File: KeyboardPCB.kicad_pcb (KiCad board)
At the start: 2 copper layers, 400.1 x 116.7 mm, 236 parts

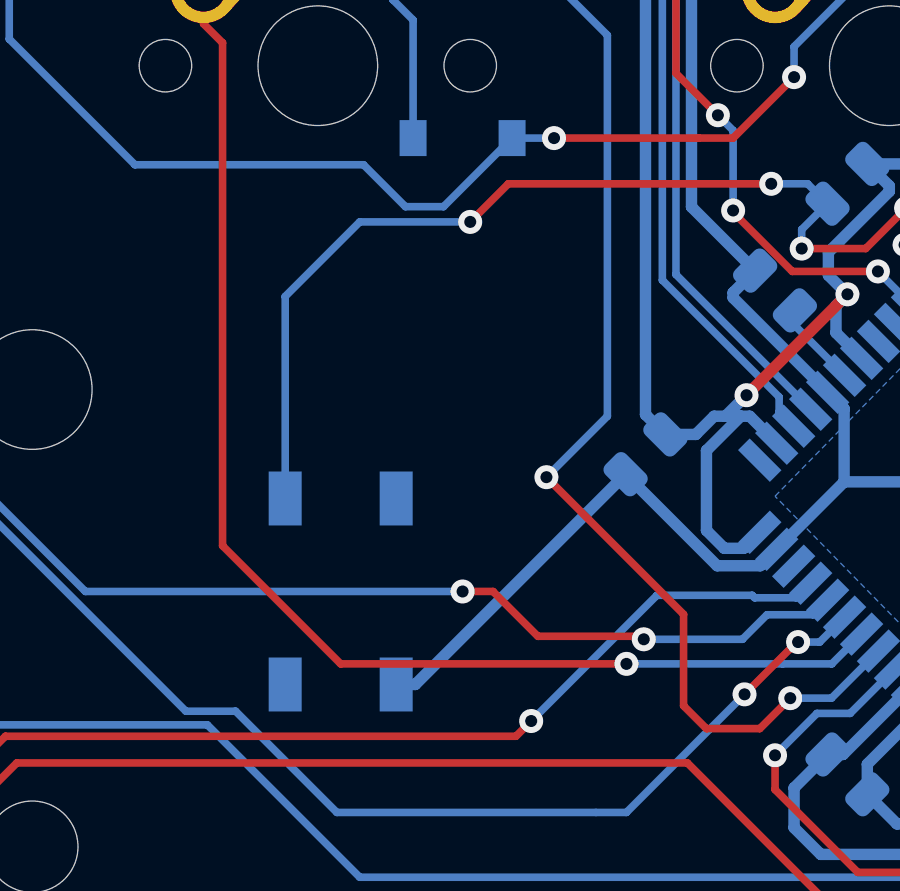
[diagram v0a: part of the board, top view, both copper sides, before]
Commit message: created custom library, added reset footprint to there
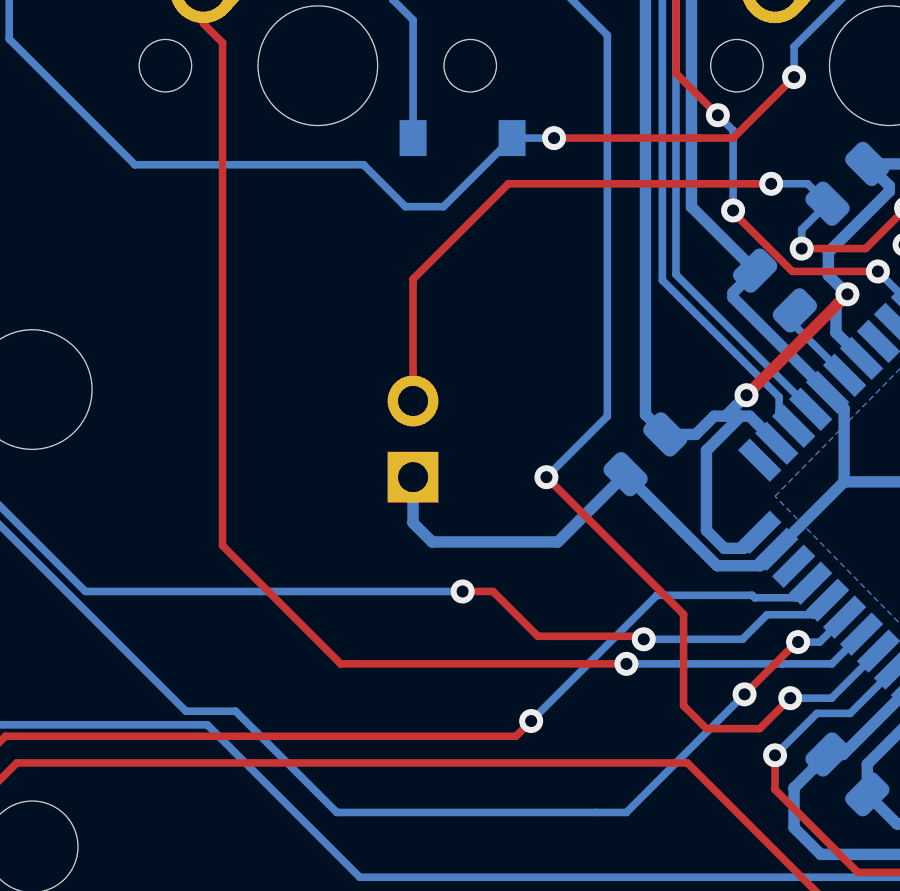
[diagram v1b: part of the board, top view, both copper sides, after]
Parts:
- SW_RESET1: footprint random-keyboard-parts:SKQG-1155865 -> random-keyboard-parts:Reset_Pretty_2pin
- moved SW_RESET1 5.08 mm to (127.6, 79.1)
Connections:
- SW_RESET1 pad 1: GND -> Net-(CONT1-Pad13)
- SW_RESET1 pad 2: Net-(CONT1-Pad13) -> GND
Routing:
- net Net-(CONT1-Pad13): track 40.5 -> 33.4 mm, vias 4 -> 3
- net GND: track 212.8 -> 212.0 mm

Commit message: fixes
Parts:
- SW_RESET1: footprint random-keyboard-parts:Reset_Pretty_2pin -> ErlMod:Reset_Pretty_2pin
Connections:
- SW_RESET1 pad 1: Net-(CONT1-Pad13) -> GND
- SW_RESET1 pad 2: GND -> Net-(CONT1-Pad13)
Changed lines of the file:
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@@
     (add_net VCC)
   )
-  (module random-keyboard-parts:Reset_Pretty_2pin (layer B.Cu)
+  (module ErlMod:Reset_Pretty_2pin (layer B.Cu)
     (at 127.635 79.121 270)
     (attr virtual)
@@
     (fp_line (start 2.5 -3.75) (end -2.5 -3.75) (layer B.SilkS) (width 0.25))
     (fp_line (start -2.5 -3.75) (end -2.5 -1.25) (layer B.SilkS) (width 0.25))
-    (pad 2 thru_hole rect (at 1.27 -2.54 270) (size 1.7 1.7) (drill 1) (layers *.Cu *.Mask)
+    (pad 1 thru_hole rect (at 1.27 -2.54 270) (size 1.7 1.7) (drill 1) (layers *.Cu *.Mask)
       (net 1 GND))
-    (pad 1 thru_hole circle (at -1.27 -2.54 270) (size 1.7 1.7) (drill 1) (layers *.Cu *.Mask)
+    (pad 2 thru_hole circle (at -1.27 -2.54 270) (size 1.7 1.7) (drill 1) (layers *.Cu *.Mask)
       (net 8 "Net-(CONT1-Pad13)"))
   )

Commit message: minor changes, added bom files
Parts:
- MX0:0_AFT1: value MX-NoLED -> MEDIA_AFT
- MX0:1_PLAY1: value MX-NoLED -> MEDIA_PLAY
- MX0:2_FWD1: value MX-NoLED -> MEDIA_FWD
- MX0:3_MUT1: value MX-NoLED -> MEDIA_MUTE
- MX0:4_VOL-1: value MX-NoLED -> MEDIA_VOLDN
- MX0:5_VOL+1: value MX-NoLED -> MEDIA_VOLUP
- MX0:6_ESC1: value MX-NoLED -> ESC
- MX0:7_F1: value MX-NoLED -> F1
- MX0:8_F2: value MX-NoLED -> F2
- MX0:9_F3: value MX-NoLED -> F3
- MX10:0_PGU1: value MX-NoLED -> PAGE_DOWN
- MX10:1_UP1: value MX-NoLED -> ARROW_UP
- MX10:4_RSH1: value MX-NoLED -> RIGHT_SHIFT
- MX10:5_/1: value MX-NoLED -> /
- MX10:6_.1: value MX-NoLED -> >
- MX10:7_,1: value MX-NoLED -> <
- MX10:8_M1: value MX-NoLED -> M
- MX10:9_N1: value MX-NoLED -> N
- MX11:0_RGT1: value MX-NoLED -> ARROW_RIGHT
- MX11:1_DWN1: value MX-NoLED -> ARROW_DOWN
- MX11:2_LFT1: value MX-NoLED -> ARROW_LEFT
- MX11:3_RCT1: value MX-NoLED -> RIGHT_CTRL
- MX11:4_MEN1: value MX-NoLED -> MENU
- MX11:5_OS1: value MX-NoLED -> RIGHT_OS
- MX11:6_AGR1: value MX-NoLED -> ALT_GR
- MX1:0_NUM1: value MX-NoLED -> NUM_LOCK
- MX1:1_NU/1: value MX-NoLED -> NUM_/
- MX1:2_NU*1: value MX-NoLED -> NUM_*
- MX1:3_NU-1: value MX-NoLED -> NUM_-
- MX1:4_TIL1: value MX-NoLED -> `
- MX1:5_1: value MX-NoLED -> 1
- MX1:6_2: value MX-NoLED -> 2
- MX1:7_3: value MX-NoLED -> 3
- MX1:8_4: value MX-NoLED -> 4
- MX1:9_5: value MX-NoLED -> 5
- MX2:0_NU7: value MX-NoLED -> NUM_7
- MX2:1_NU8: value MX-NoLED -> NUM_8
- MX2:2_NU9: value MX-NoLED -> NUM_9
- MX2:3_NU+1: value MX-NoLED -> NUM_+
- MX2:4_TAB1: value MX-NoLED -> TAB
- MX2:5_Q1: value MX-NoLED -> Q
- MX2:6_W1: value MX-NoLED -> W
- MX2:7_E1: value MX-NoLED -> E
- MX2:8_R1: value MX-NoLED -> R
- MX2:9_T1: value MX-NoLED -> T
- MX3:0_NU4: value MX-NoLED -> NUM_4
- MX3:1_NU5: value MX-NoLED -> NUM_5
- MX3:2_NU6: value MX-NoLED -> NUM_6
- MX3:4_CAP1: value MX-NoLED -> CAPS
- MX3:5_A1: value MX-NoLED -> A
- MX3:6_S1: value MX-NoLED -> S
- MX3:7_D1: value MX-NoLED -> D
- MX3:8_F1: value MX-NoLED -> F
- MX3:9_G1: value MX-NoLED -> G
- MX4:0_NU1: value MX-NoLED -> NUM_1
- MX4:1_NU2: value MX-NoLED -> NUM_2
- MX4:2_NU3: value MX-NoLED -> NUM_3
- MX4:3_NEN1: value MX-NoLED -> NUM_ENTER
- MX4:4_LSH1: value MX-NoLED -> LEFT_SHIFT
- MX4:5_Z1: value MX-NoLED -> Z
- MX4:6_X1: value MX-NoLED -> X
- MX4:7_C1: value MX-NoLED -> C
- MX4:8_V1: value MX-NoLED -> V
- MX4:9_B1: value MX-NoLED -> B
- MX5:0_NU0: value MX-NoLED -> NUM_0
- MX5:2_NUD1: value MX-NoLED -> NUM_DEL
- MX5:3_LCT1: value MX-NoLED -> LEFT_CTRL
- MX5:4_OS1: value MX-NoLED -> LEFT_OS
- MX5:5_LAL1: value MX-NoLED -> LEFT_ALT
- MX5:9_SPC1: value MX-NoLED -> SPACE
- MX6:0_PRT1: value MX-NoLED -> PRINT
- MX6:1_F12: value MX-NoLED -> F12
- MX6:2_F11: value MX-NoLED -> F11
- MX6:3_F10: value MX-NoLED -> F10
- MX6:4_F9: value MX-NoLED -> F9
- MX6:5_F8: value MX-NoLED -> F8
- MX6:6_F7: value MX-NoLED -> F7
- MX6:7_F6: value MX-NoLED -> F6
- MX6:8_F5: value MX-NoLED -> F5
- MX6:9_F4: value MX-NoLED -> F4
- MX7:0_HOM1: value MX-NoLED -> HOME
- MX7:1_INS1: value MX-NoLED -> INSERT
- MX7:2_BSP1: value MX-NoLED -> BACKSPACE
- MX7:3_=1: value MX-NoLED -> = +
- MX7:4_-1: value MX-NoLED -> - _
- MX7:5_0: value MX-NoLED -> 0
- MX7:6_9: value MX-NoLED -> 9
- MX7:7_8: value MX-NoLED -> 8
- MX7:8_7: value MX-NoLED -> 7
- MX7:9_6: value MX-NoLED -> 6
- MX8:0_END1: value MX-NoLED -> END
- MX8:1_DEL1: value MX-NoLED -> DELETE
- MX8:2_\1: value MX-NoLED -> \ |
- MX8:3_]1: value MX-NoLED -> ]
- MX8:4_[1: value MX-NoLED -> [
- MX8:5_P1: value MX-NoLED -> P
- MX8:6_O1: value MX-NoLED -> O
- MX8:7_I1: value MX-NoLED -> I
- MX8:8_U1: value MX-NoLED -> U
- MX8:9_Y1: value MX-NoLED -> Y
- MX9:0_PGU1: value MX-NoLED -> PAGE_UP
- MX9:1_SLK1: value MX-NoLED -> SCROLL_LOCK
- MX9:2_PUS1: value MX-NoLED -> PAUSE
- MX9:3_ENT1: value MX-NoLED -> ENTER
- MX9:4_'1: value MX-NoLED -> '
- MX9:5_;1: value MX-NoLED -> ;
- MX9:6_L1: value MX-NoLED -> L
- MX9:7_K1: value MX-NoLED -> K
- MX9:8_J1: value MX-NoLED -> J
- MX9:9_H1: value MX-NoLED -> H

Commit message: Added silkscreen button designations
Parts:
- added ?: , , F.Cu at (65.7, 224.3)
- moved D0:5 1.93 mm to (72.2, -5.56)
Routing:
- net COL2: track 870.8 -> 882.2 mm, vias 15 -> 17
- net COL6: track 474.7 -> 466.5 mm
- net +5V: track 181.6 -> 183.3 mm
- net Net-(D0:5-Pad2): track 11.5 -> 10.0 mm
- net COL3: track 663.7 -> 662.6 mm
- net COL7: track 362.6 -> 361.5 mm
- net COL8: track 349.9 -> 349.3 mm
- net ROW3: track 253.4 -> 252.9 mm
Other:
- board text added: "'"
- board text added: "- _"
- board text added: "/"
- board text added: "0"
- board text added: "1"
- board text added: "2"
- board text added: "3"
- board text added: "4"
- board text added: "5"
- board text added: "6"
- board text added: "7"
- board text added: "8"
- board text added: "9"
- board text added: ";"
- board text added: "<"
- board text added: "= +"
- board text added: ">"
- board text added: "A"
- board text added: "ALT_GR"
- board text added: "ARROW_DOWN"
- board text added: "ARROW_LEFT"
- board text added: "ARROW_RIGHT"
- board text added: "ARROW_UP"
- board text added: "B"
- board text added: "BACKSPACE"
- board text added: "C"
- board text added: "CAPS"
- board text added: "D"
- board text added: "DELETE"
- board text added: "E"
- board text added: "END"
- board text added: "ENTER"
- board text added: "ESC"
- board text added: "F"
- board text added: "F1"
- board text added: "F10"
- board text added: "F11"
- board text added: "F12"
- board text added: "F2"
- board text added: "F3"
- board text added: "F4"
- board text added: "F5"
- board text added: "F6"
- board text added: "F7"
- board text added: "F8"
- board text added: "F9"
- board text added: "G"
- board text added: "H"
- board text added: "HOME"
- board text added: "I"
- board text added: "INSERT"
- board text added: "J"
- board text added: "K"
- board text added: "L"
- board text added: "LEFT_ALT"
- board text added: "LEFT_CTRL"
- board text added: "LEFT_OS"
- board text added: "LEFT_SHIFT"
- board text added: "M"
- board text added: "MEDAI_MUTE"
- board text added: "MEDAI_VOLUP"
- board text added: "MEDIA_AFT"
- board text added: "MEDIA_FWD"
- board text added: "MEDIA_PLAY"
- board text added: "MEDIA_VOLDN"
- board text added: "MENU"
- board text added: "N"
- board text added: "NUM_*"
- board text added: "NUM_+"
- board text added: "NUM_-"
- board text added: "NUM_/"
- board text added: "NUM_0"
- board text added: "NUM_1"
- board text added: "NUM_2"
- board text added: "NUM_3"
- board text added: "NUM_4"
- board text added: "NUM_5"
- board text added: "NUM_6"
- board text added: "NUM_7"
- board text added: "NUM_8"
- board text added: "NUM_9"
- board text added: "NUM_DEL"
- board text added: "NUM_ENTER"
- board text added: "NUM_LOCK"
- board text added: "O"
- board text added: "P"
- board text added: "PAGE_DOWN"
- board text added: "PAGE_UP"
- board text added: "PAUSE"
- board text added: "PRINT"
- board text added: "Q"
- board text added: "R"
- board text added: "RIGHT_CTRL"
- board text added: "RIGHT_OS"
- board text added: "RIGHT_SHIFT"
- board text added: "S"
- board text added: "SCROLL_LOCK"
- board text added: "SPACE"
- board text added: "T"
- board text added: "TAB"
- board text added: "U"
- board text added: "W"
- board text added: "X"
- board text added: "Y"
- board text added: "Z"
- board text added: "["
- board text added: "\ |"
- board text added: "]"
- board text added: "`"

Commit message: routing fixes
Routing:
- net ROW2: track 265.5 -> 262.3 mm
- net ROW7: track 280.5 -> 279.0 mm
- net COL5: track 521.9 -> 521.3 mm
- net COL9: track 280.6 -> 280.0 mm

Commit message: Changed switch footprint to mx only, general tidy up
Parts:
- removed ?: , 
- MX0:0_AFT1, MX0:1_PLAY1, MX0:2_FWD1, MX0:3_MUT1, MX0:4_VOL-1, MX0:5_VOL+1, MX0:6_ESC1, MX0:7_F1, MX0:8_F2, MX0:9_F3, MX10:0_PGU1, MX10:1_UP1, MX10:5_/1, MX10:6_.1, MX10:7_,1, MX10:8_M1, MX10:9_N1, MX11:0_RGT1, MX11:1_DWN1, MX11:2_LFT1, MX11:3_RCT1, MX11:4_MEN1, MX11:5_OS1, MX11:6_AGR1, MX1:0_NUM1, MX1:1_NU/1, MX1:2_NU*1, MX1:3_NU-1, MX1:4_TIL1, MX1:5_1, MX1:6_2, MX1:7_3, MX1:8_4, MX1:9_5, MX2:0_NU7, MX2:1_NU8, MX2:2_NU9, MX2:5_Q1, MX2:6_W1, MX2:7_E1, MX2:8_R1, MX2:9_T1, MX3:0_NU4, MX3:1_NU5, MX3:2_NU6, MX3:5_A1, MX3:6_S1, MX3:7_D1, MX3:8_F1, MX3:9_G1, MX4:0_NU1, MX4:1_NU2, MX4:2_NU3, MX4:5_Z1, MX4:6_X1, MX4:7_C1, MX4:8_V1, MX4:9_B1, MX5:2_NUD1, MX6:0_PRT1, MX6:1_F12, MX6:2_F11, MX6:3_F10, MX6:4_F9, MX6:5_F8, MX6:6_F7, MX6:7_F6, MX6:8_F5, MX6:9_F4, MX7:0_HOM1, MX7:1_INS1, MX7:3_=1, MX7:4_-1, MX7:5_0, MX7:6_9, MX7:7_8, MX7:8_7, MX7:9_6, MX8:0_END1, MX8:1_DEL1, MX8:3_]1, MX8:4_[1, MX8:5_P1, MX8:6_O1, MX8:7_I1, MX8:8_U1, MX8:9_Y1, MX9:0_PGU1, MX9:1_SLK1, MX9:2_PUS1, MX9:4_'1, MX9:5_;1, MX9:6_L1, MX9:7_K1, MX9:8_J1, MX9:9_H1: footprint MX_Alps_Hybrid:MX-1U-NoLED -> MX_Only:MXOnly-1U-NoLED
- MX10:4_RSH1: footprint MX_Alps_Hybrid:MX-2.75U-NoLED -> MX_Only:MXOnly-2.75U-NoLED
- MX2:3_NU+1, MX4:3_NEN1, MX7:2_BSP1: footprint MX_Alps_Hybrid:MX-2U-NoLED -> MX_Only:MXOnly-2U-NoLED
- MX2:4_TAB1: footprint MX_Alps_Hybrid:MX-1.5U-NoLED -> MX_Only:MXOnly-1.5U-NoLED
- MX3:4_CAP1: footprint MX_Alps_Hybrid:MX-1.75U-NoLED -> MX_Only:MXOnly-1.75U-NoLED
- MX4:4_LSH1, MX9:3_ENT1: footprint MX_Alps_Hybrid:MX-2.25U-NoLED -> MX_Only:MXOnly-2.25U-NoLED
- MX5:0_NU0: footprint MX_Alps_Hybrid:MX-2U-ReversedStabilizers-NoLED -> MX_Only:MXOnly-2U-ReversedStabilizers-NoLED
- MX5:3_LCT1, MX5:4_OS1, MX5:5_LAL1: footprint MX_Alps_Hybrid:MX-1.25U-NoLED -> MX_Only:MXOnly-1.25U-NoLED
- MX5:9_SPC1: footprint MX_Alps_Hybrid:MX-6.25U-ReversedStabilizers-NoLED -> MX_Only:MXOnly-6.25U-ReversedStabilizers-NoLED
- MX8:2_\1: footprint MX_Alps_Hybrid:MX-1.5U-NoLED -> MX_Only:MXOnly-1U-NoLED
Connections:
- CONT1 pad 38: COL7 -> COL6
- CONT1 pad 39: COL6 -> COL7
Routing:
- net COL8: track 349.3 -> 334.6 mm
- net COL4: track 596.2 -> 605.0 mm
- net COL1: track 719.4 -> 726.7 mm, vias 4 -> 0
- net COL6: track 466.5 -> 473.3 mm, vias 6 -> 4
- net COL0: track 813.9 -> 820.3 mm, vias 15 -> 13
- net COL9: track 280.0 -> 286.4 mm
- net COL5: track 521.3 -> 527.3 mm, vias 5 -> 3
- net COL3: track 662.6 -> 665.6 mm
- net Net-(D7:0-Pad2): track 13.0 -> 10.5 mm, vias 2 -> 1
- net COL7: track 361.2 -> 359.7 mm
- net COL2: track 882.2 -> 883.1 mm, vias 17 -> 14
- net ROW8: track 252.2 -> 252.8 mm, vias 4 -> 0
- net ROW10: track 209.5 -> 209.3 mm, vias 2 -> 0
- net ROW9: track 291.4 -> 291.6 mm, vias 10 -> 6
- net ROW2: track 262.3 -> 262.4 mm, vias 6 -> 4
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
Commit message: further trace fixes
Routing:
- net Net-(D8:0-Pad2): track 29.7 -> 10.5 mm
- net Net-(D9:0-Pad2): track 30.1 -> 11.5 mm
- net COL3: track 665.6 -> 669.8 mm, vias 7 -> 5
- net COL5: track 527.3 -> 531.1 mm
- net COL2: track 883.1 -> 886.6 mm, vias 14 -> 11
- net COL4: track 605.0 -> 608.3 mm
- net COL1: track 726.7 -> 729.4 mm
- net COL8: track 334.6 -> 337.0 mm
- net COL6: track 473.3 -> 474.9 mm, vias 4 -> 3
- net COL0: track 820.3 -> 821.7 mm
- net ROW9: track 291.6 -> 290.5 mm, vias 6 -> 4
- net COL9: track 286.4 -> 285.4 mm
- net COL7: track 359.7 -> 360.1 mm, vias 5 -> 4

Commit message: added new usb footprint, attached it
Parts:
- USB1: value Molex-0548190589 -> Molex-0548190572; footprint random-keyboard-parts:Molex-0548190589 -> ErlMod:Molex-0548190572
- moved USB1 1.02 mm to (113.7, -18.9), turned to 180 degrees
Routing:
- net D+: track 19.4 -> 21.8 mm
- net VCC: track 13.4 -> 15.8 mm
- net D-: track 19.3 -> 21.7 mm
- net GND: track 212.0 -> 214.4 mm
- net COL0: track 821.7 -> 821.2 mm
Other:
- board size 400.1 x 116.7 mm -> 400.1 x 118.5 mm
